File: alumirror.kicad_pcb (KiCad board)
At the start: 2 copper layers, 142.9 x 87.2 mm, 77 parts, among them J1 USB_C_Receptacle_USB2.0_16P_2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, J2 USB_C_Receptacle_USB2.0_16P_2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, K00 PG1350, K01 PG1350, K02 PG1350, K03 PG1350, K04 PG1350, K05 PG1350, K10 PG1350, K11 PG1350, K12 PG1350, K13 PG1350, K14 PG1350, K15 PG1350, K20 PG1350, K21 PG1350, K22 PG1350, K23 PG1350, K24 PG1350, K25 PG1350_1½U, K30 PG1350_1½U, K31 PG1350/SKQUCAA010, SW1 BOOT, U1 CH552T, U2 CH552T, U3 USBLC6-2P6, U4 USBLC6-2P6

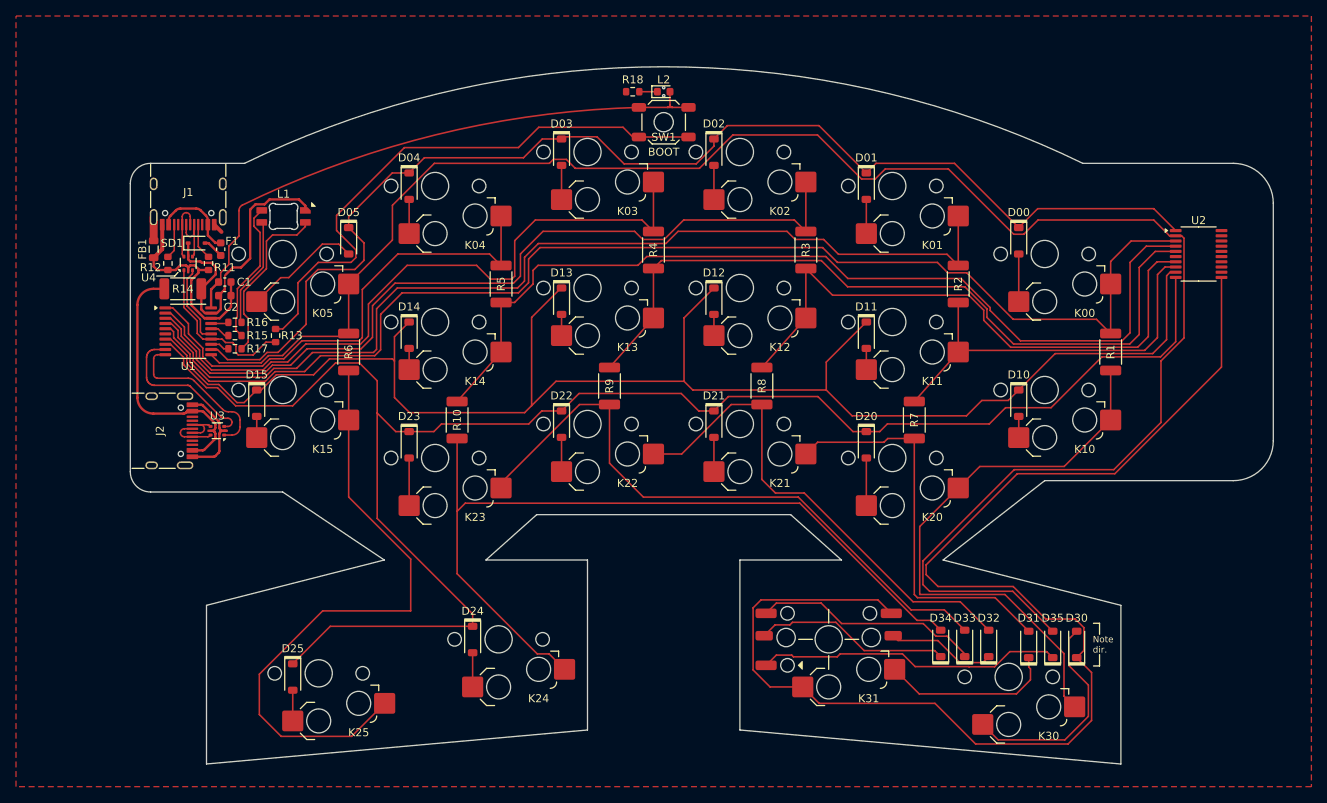
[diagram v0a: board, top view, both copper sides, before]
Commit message: Add righthand active components
Routing is **very** rough
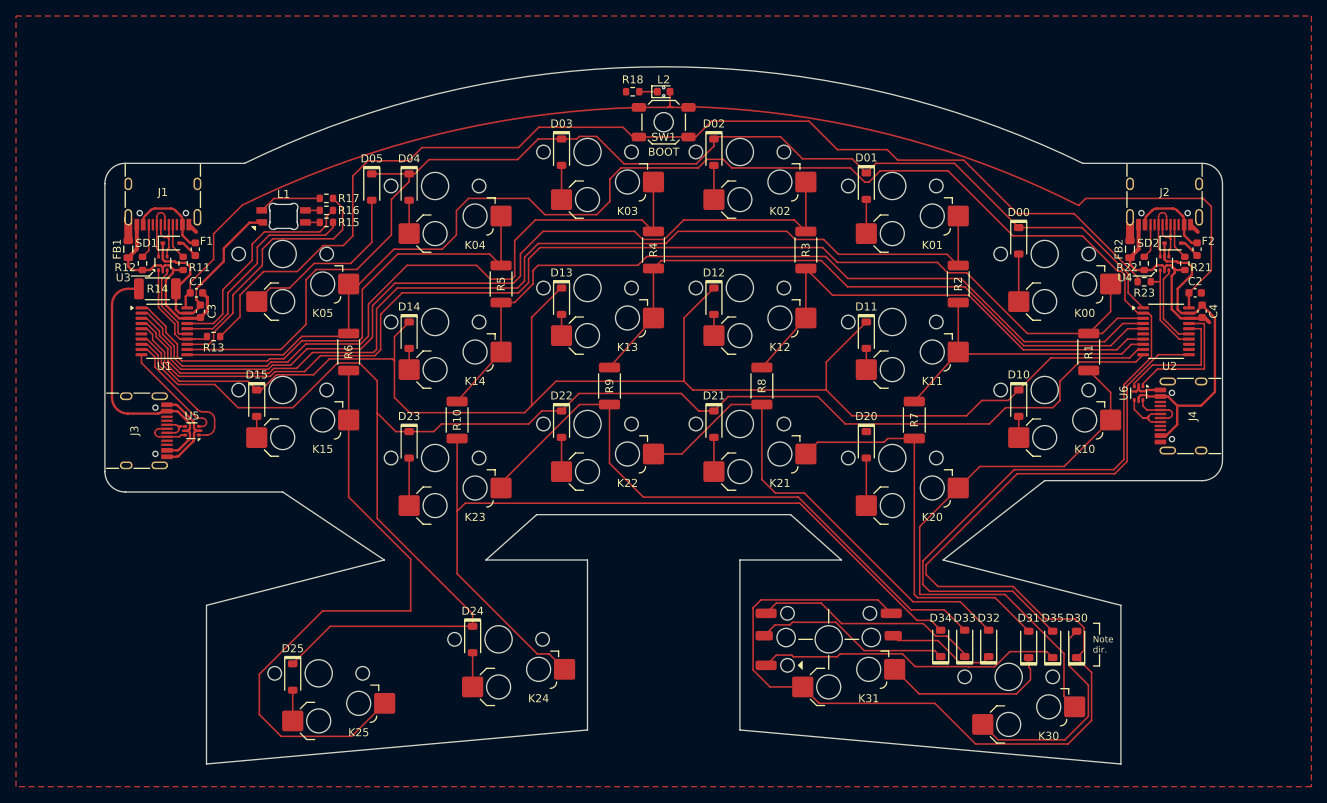
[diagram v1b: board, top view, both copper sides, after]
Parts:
- added C2: 100nF, Capacitor_SMD:C_0603_1608Metric, F.Cu at (218.8, 57.3)
- added C4: 100nF, Capacitor_SMD:C_0603_1608Metric, F.Cu at (219.7, 59.6)
- added F2: 500mA, Fuse:Fuse_0603_1608Metric, F.Cu at (219.1, 51.8)
- added FB2: FerriteBead, Inductor_SMD:L_0805_2012Metric, F.Cu at (210.7, 51.8)
- added J2: USB_C_Receptacle_USB2.0_16P_2SH, Project Library:USB_C_Receptacle_HRO_TYPE-C-31-M-12, F.Cu at (215.0, 44.7)
- added J4: USB_C_Receptacle_USB2.0_16P_2SH, Project Library:USB_C_Receptacle_HRO_TYPE-C-31-M-12, F.Cu at (218.5, 72.7)
- added NT2: NetTie_2, Project Library:NetTie-2_SMD_Pad0.2mm, F.Cu at (213.9, 55.9)
- added R21: 5k1, Project Library:R_0603_1608Metric_Mod, F.Cu at (217.5, 53.6)
- added R22: 5k1, Project Library:R_0603_1608Metric_Mod, F.Cu at (212.5, 53.6)
- added R23: 10k, Project Library:R_0603_1608Metric_Mod, F.Cu at (212.5, 55.9)
- added SD2: PMEG2010EA, Diode_SMD:D_SOD-323, F.Cu at (216.1, 51.1)
- added U4: USBLC6-2P6, Package_TO_SOT_SMD:SOT-666, F.Cu at (215.0, 53.6)
- added U6: USBLC6-2P6, Package_TO_SOT_SMD:SOT-666, F.Cu at (211.8, 69.8)
- moved R17 22.0 mm to (110.2, 45.5), turned to 180 degrees
- moved R15 18.2 mm to (110.2, 48.5), turned to 180 degrees
- moved R16 18.1 mm to (110.2, 47.0), turned to 180 degrees
- moved U2 10.5 mm to (215.2, 62.1)
- moved R13 7.75 mm to (96.1, 62.7), turned to 0 degrees
- moved D05 7.31 mm to (115.9, 44.1)
- moved C1 3.79 mm to (94.0, 57.3)
- moved C3 3.62 mm to (94.5, 59.6), turned to -90 degrees
- moved F1 3.18 mm to (93.9, 51.8)
- moved FB1 3.18 mm to (85.5, 51.8)
- moved R11 3.18 mm to (92.3, 53.6)
- moved R12 3.18 mm to (87.2, 53.6)
- moved J1 3.17 mm to (89.8, 44.7)
- moved J3 3.17 mm to (86.3, 74.5)
- moved R14 3.17 mm to (89.1, 56.8)
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- renumbered C2 to C3, J2 to J3, U4 to U3, U3 to U5
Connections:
- net /BOOT renamed BOOT
- J3 pad A6: RX_PL -> TX_PL
- J3 pad A7: TX_PL -> RX_PL
- J3 pad B6: RX_PL -> TX_PL
- J3 pad B7: TX_PL -> RX_PL
- U2 pad 14: unconnected-(U2-P3.6/UDP-Pad14) -> USB_R+
- U2 pad 15: unconnected-(U2-P3.7/UDM-Pad15) -> USB_R-
- U2 pad 18: unconnected-(U2-GND-Pad18) -> GND
- U2 pad 19: unconnected-(U2-VCC-Pad19) -> VCC_R
- U2 pad 20: unconnected-(U2-V33-Pad20) -> +3V3
- U5 pad 1: RX_L -> TX_L
- U5 pad 3: TX_L -> RX_L
- U5 pad 4: TX_PL -> RX_PL
- U5 pad 6: RX_PL -> TX_PL
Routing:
- net BOOT: track 70.6 -> 140.7 mm
- net VCC_R: track 0.00 -> 43.4 mm
- net +3V3: track 20.9 -> 54.2 mm
- net LED_B: track 2.51 -> 33.0 mm
- net GND: track 41.7 -> 69.7 mm
- net LED_G: track 2.01 -> 27.8 mm
- net LED_R: track 2.51 -> 27.0 mm
- net RX_R: track 0.00 -> 16.4 mm
- net Net-(L1-RK): track 17.9 -> 1.80 mm
- net TX_R: track 0.00 -> 15.8 mm
- net Net-(L1-BK): track 21.3 -> 7.84 mm
- net Col3R: track 94.2 -> 80.8 mm
- net Col2R: track 74.8 -> 61.4 mm
- net Col4R: track 116.8 -> 103.5 mm
- net Col1R: track 50.2 -> 38.2 mm
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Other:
- board size 142.9 x 87.2 mm -> 139.7 x 87.2 mm

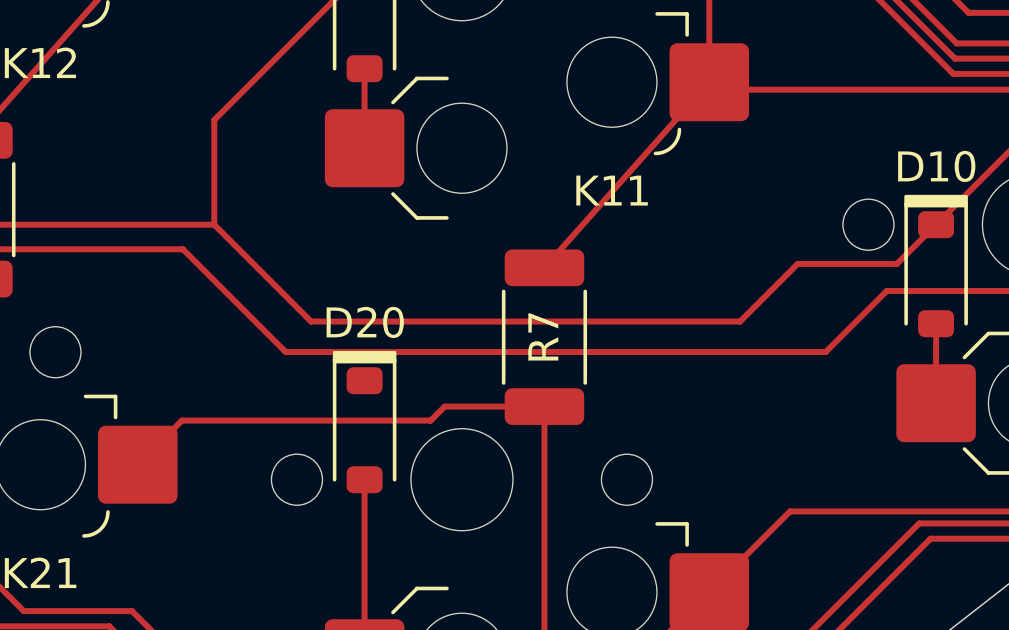
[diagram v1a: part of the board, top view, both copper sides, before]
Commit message: Tidy schematic
Matrix is broken out into a separate sheet
Controller components are more organised
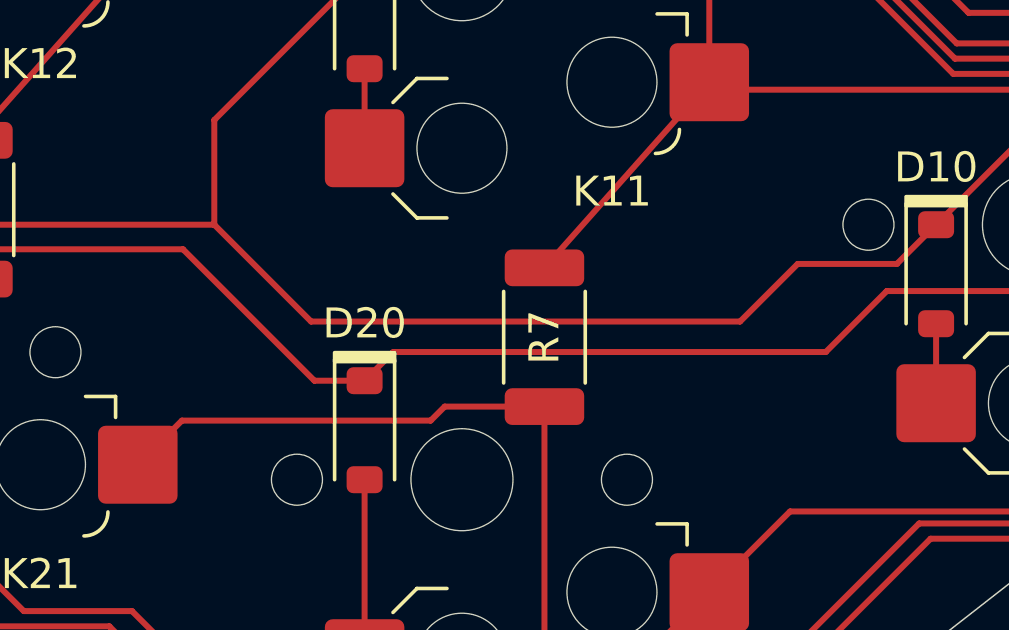
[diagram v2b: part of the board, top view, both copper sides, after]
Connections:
- net /Col0' renamed Col0T
- net /Col1R' renamed Col1RT
- net /Col2R' renamed Col2RT
- net /Col3R' renamed Col3RT
- net /Col4R' renamed Col4T
- net /Col5' renamed Col5T
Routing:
- net Row2: track 203.7 -> 204.5 mm

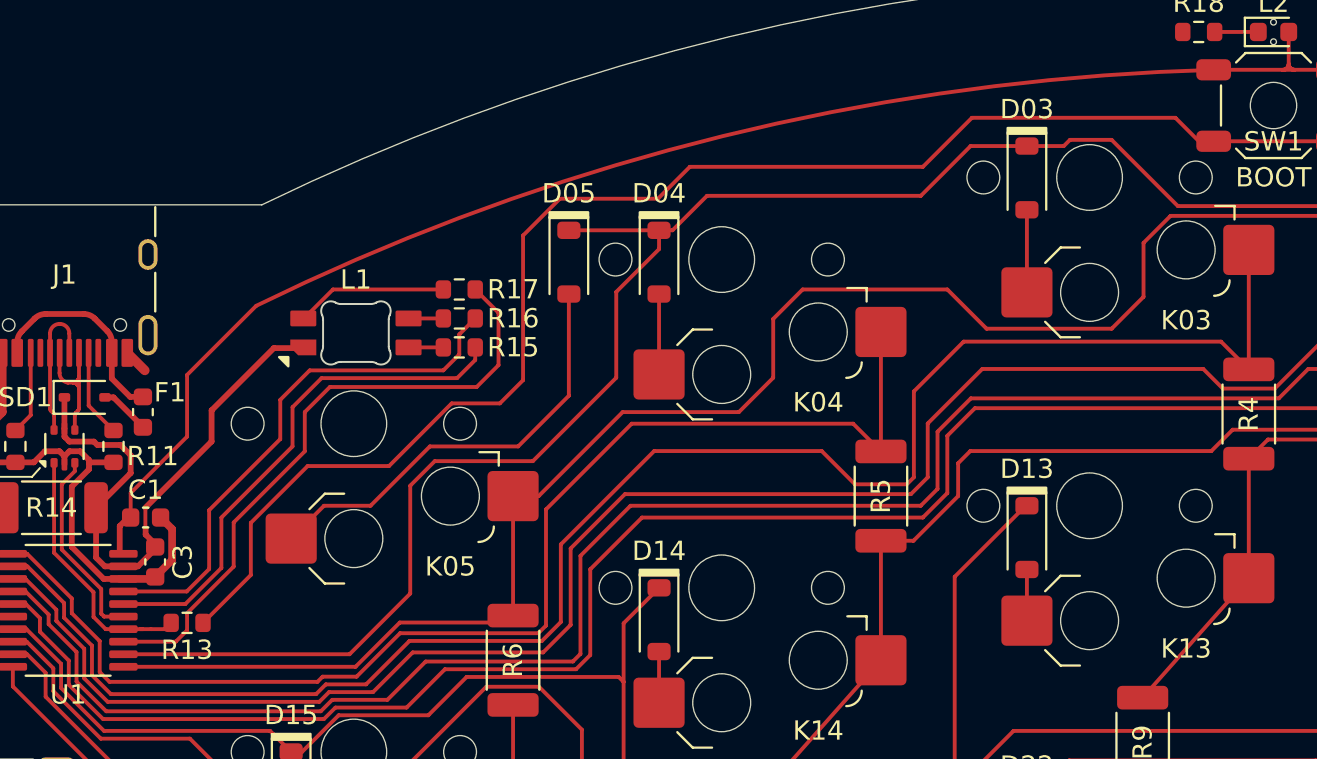
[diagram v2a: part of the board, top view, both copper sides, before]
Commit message: Relocate lefthand capacitors
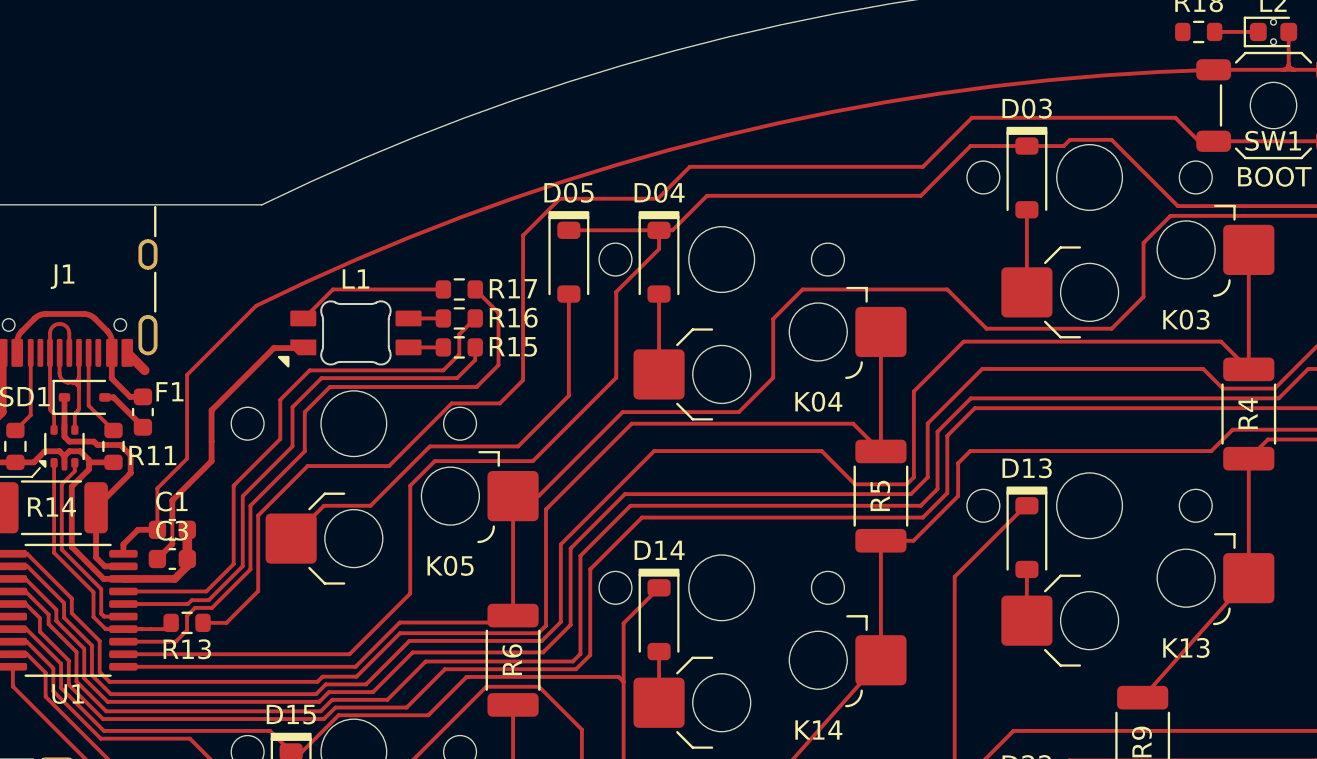
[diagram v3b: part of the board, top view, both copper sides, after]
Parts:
- moved C1 1.52 mm to (95.4, 57.9)
- moved C3 0.90 mm to (95.4, 59.4), turned to 0 degrees
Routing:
- net VCC_L: track 30.2 -> 28.3 mm
- net BOOT: track 140.7 -> 141.4 mm
- net LED_R: track 27.0 -> 27.6 mm
- net LED_G: track 27.8 -> 28.4 mm
- net LED_B: track 33.0 -> 33.5 mm
- net +3V3: track 54.2 -> 54.7 mm

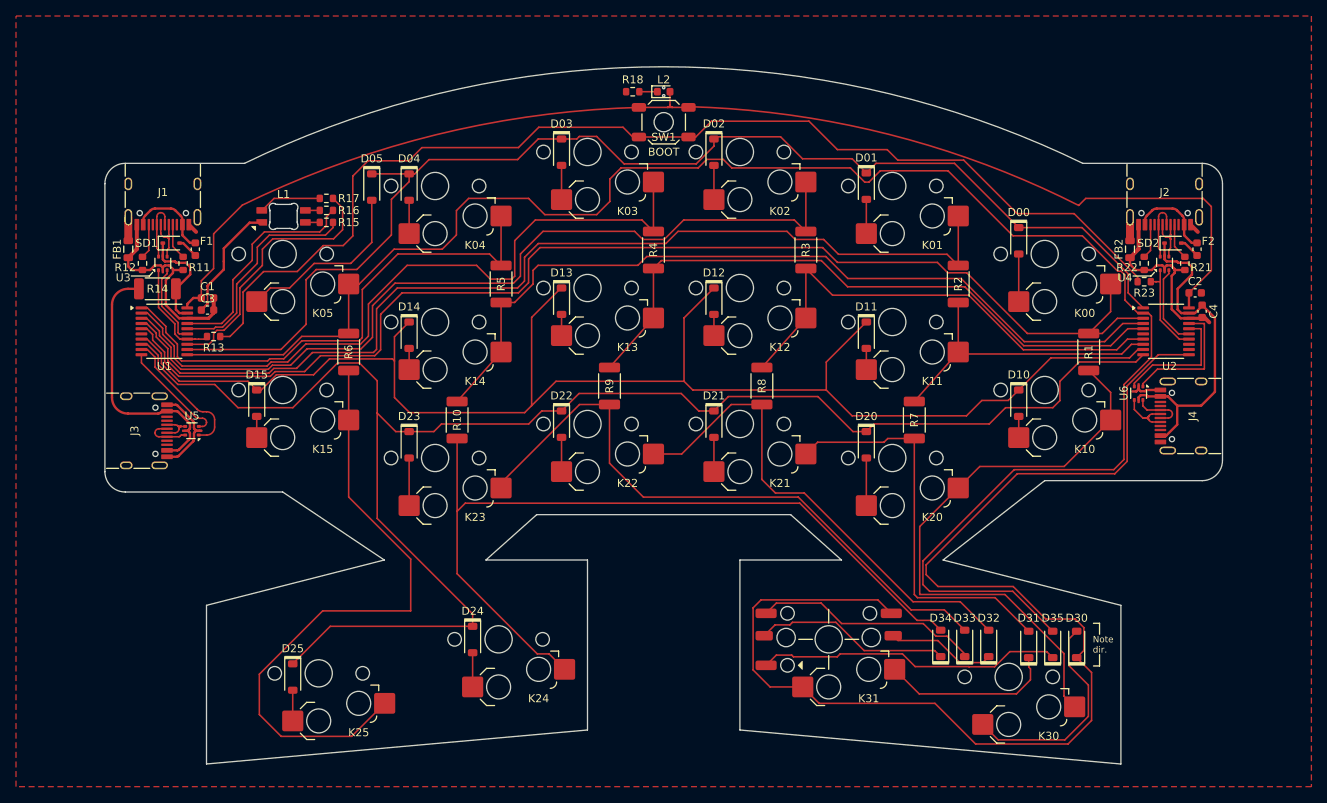
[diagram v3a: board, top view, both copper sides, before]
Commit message: Rearrange components for better layout
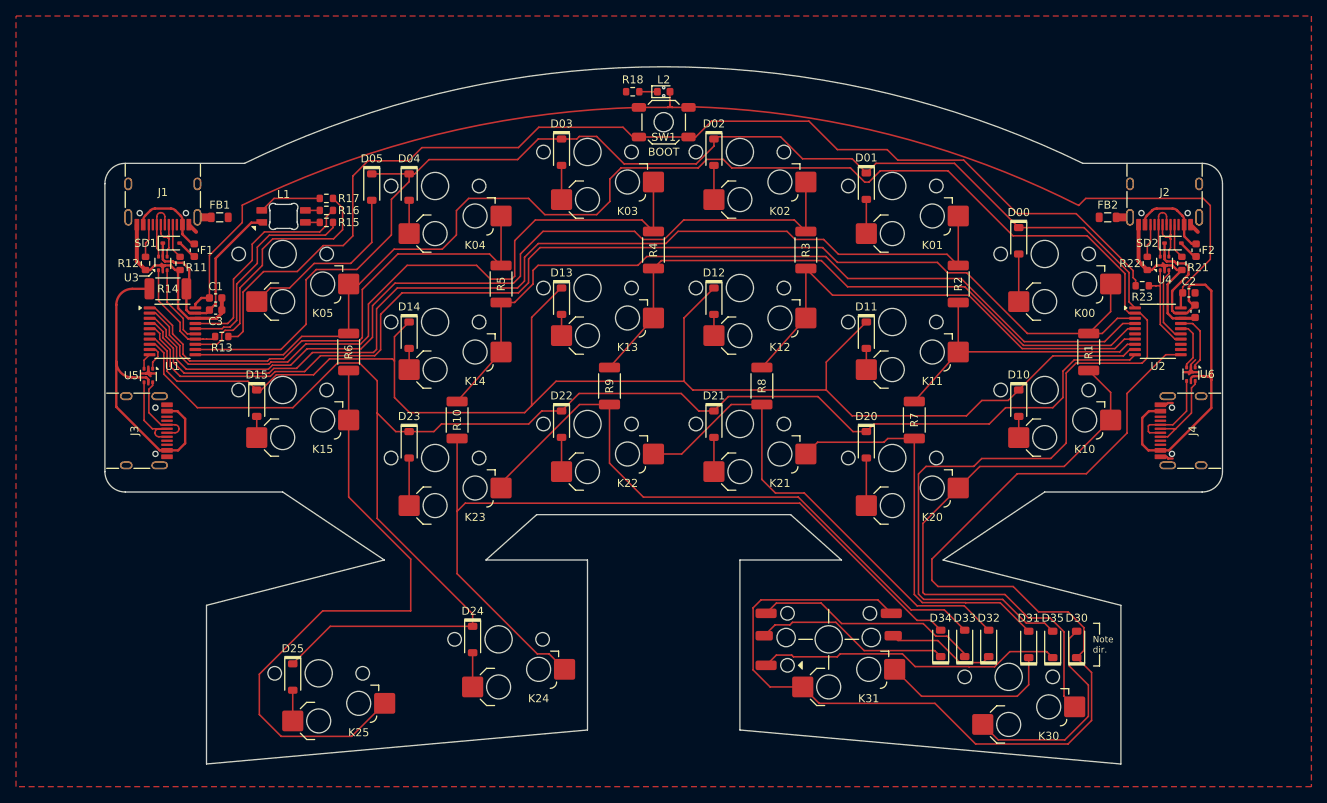
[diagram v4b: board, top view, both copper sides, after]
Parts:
- moved FB1 12.1 mm to (96.9, 47.8), turned to 0 degrees
- moved U5 8.80 mm to (88.0, 67.6), turned to -90 degrees
- moved U6 6.96 mm to (218.3, 67.4)
- moved FB2 4.86 mm to (207.9, 47.8), turned to 180 degrees
- moved J4 1.84 mm to (218.5, 74.5)
- moved R14 1.31 mm to (90.4, 56.8)
- moved U2 1.02 mm to (214.2, 62.1)
- moved C1 1.02 mm to (96.4, 57.9)
- moved C3 1.02 mm to (96.4, 59.4)
- moved NT1 1.02 mm to (94.8, 63.1)
- moved R13 1.02 mm to (97.2, 62.7)
- moved U1 1.02 mm to (91.0, 62.1)
- moved C4 0.88 mm to (218.8, 59.6)
- moved C2 0.79 mm to (218.0, 57.3)
- moved R23 0.57 mm to (212.2, 56.4)
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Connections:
- J1 pad S1: Net-(FB1-Pad1) -> unconnected-(J1-SHIELD-PadS1)
- J1 pad S2: unconnected-(J1-SHIELD-PadS2)_2 -> Net-(FB1-Pad1)
- J3 pad A6: TX_PL -> RX_PL
- J3 pad A7: RX_PL -> TX_PL
- J3 pad B6: TX_PL -> RX_PL
- J3 pad B7: RX_PL -> TX_PL
- J4 pad A6: RX_PR -> TX_PR
- J4 pad A7: TX_PR -> RX_PR
- J4 pad B6: RX_PR -> TX_PR
- J4 pad B7: TX_PR -> RX_PR
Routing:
- net TX_L: track 17.0 -> 3.54 mm
- net VCC_R: track 43.4 -> 56.4 mm
- net RX_L: track 13.5 -> 2.03 mm
- net TX_R: track 15.8 -> 6.34 mm
- net GND: track 69.8 -> 60.9 mm
- net RX_R: track 16.4 -> 7.60 mm
- net RX_PL: track 4.03 -> 11.6 mm
- net VCC_L': track 33.5 -> 40.4 mm
- net Col5: track 221.3 -> 227.6 mm
- net RX_PR: track 6.67 -> 11.2 mm
- net TX_PL: track 5.88 -> 10.4 mm
- net Row3R: track 159.2 -> 155.0 mm
- net TX_PR: track 7.75 -> 11.2 mm
- net Row0: track 156.2 -> 154.6 mm
- net Col0: track 152.6 -> 151.0 mm
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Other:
- outline, holes or cut-outs redrawn
